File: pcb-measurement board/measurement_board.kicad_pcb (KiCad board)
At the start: 4 copper layers, 60 x 46 mm, 100 parts, among them P1 HDR DUAL ROW, P2 CONN_02X15, P3 CONN_02X13, P4 CONN_02X05, P5 CONN_02X05, Q1 Si1101X, Q2 2N7002, U1 NX3L4051, U10 TLV1G125, U11 NX3L4051, U12 MSP430G2955, U13 AD8603, U14 TLV1G125, U15 MCP4921, U16 AD8293, U17 NX3L4051, U18 NX3L4051, U19 QS4A110, U2 TPS73133, U20 QS4A110, U21 TLV1G125, U22 TLV1G125, U23 AD7683, U3 74CBTLV3253, U4 NX3L4051, U5 TPS73125, U6 AD8603, U7 MCP4921, U8 NX3L4051, U9 TLV1G125

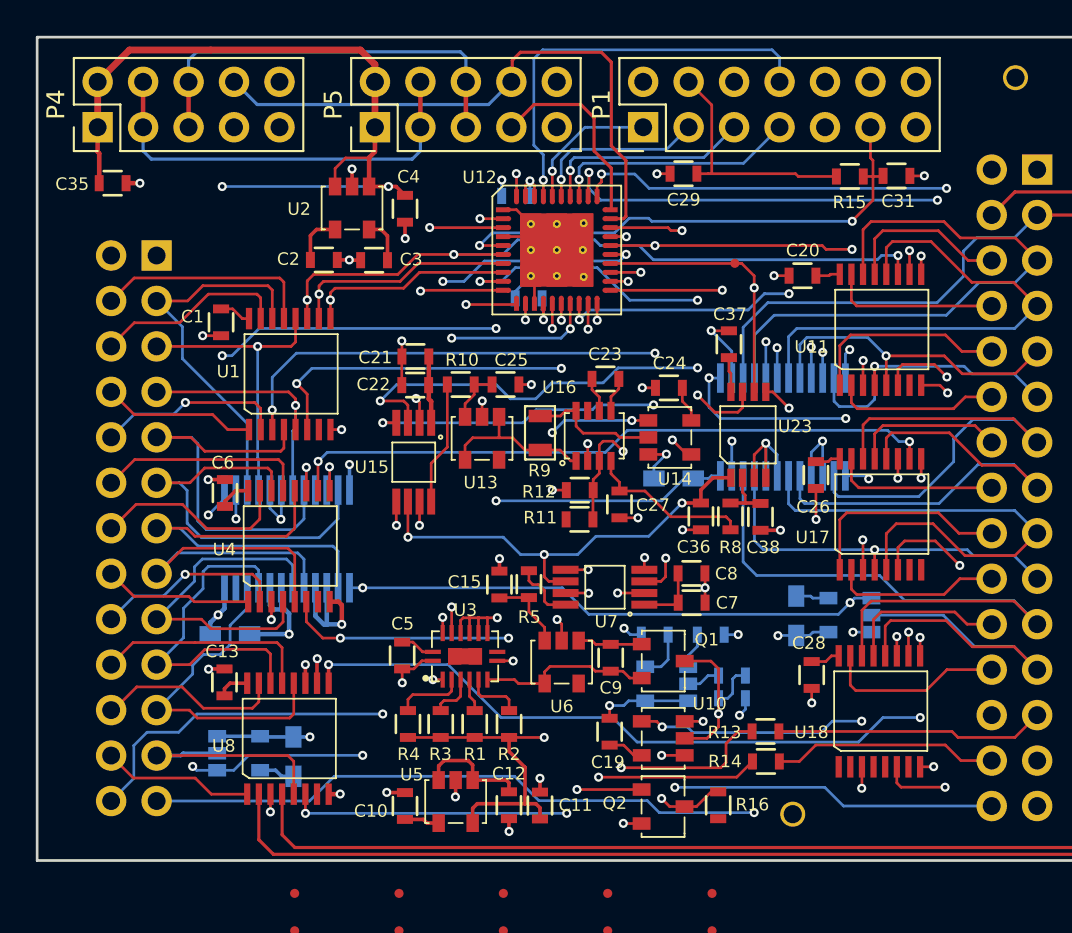
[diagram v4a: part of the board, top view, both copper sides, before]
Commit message: -nearing completion of measurement board layout -routed most signal traces, just need to add testpoints and fix DRC voilations -changed MSP430 programming connector from 2x7 header to 10-pin flex cable connector
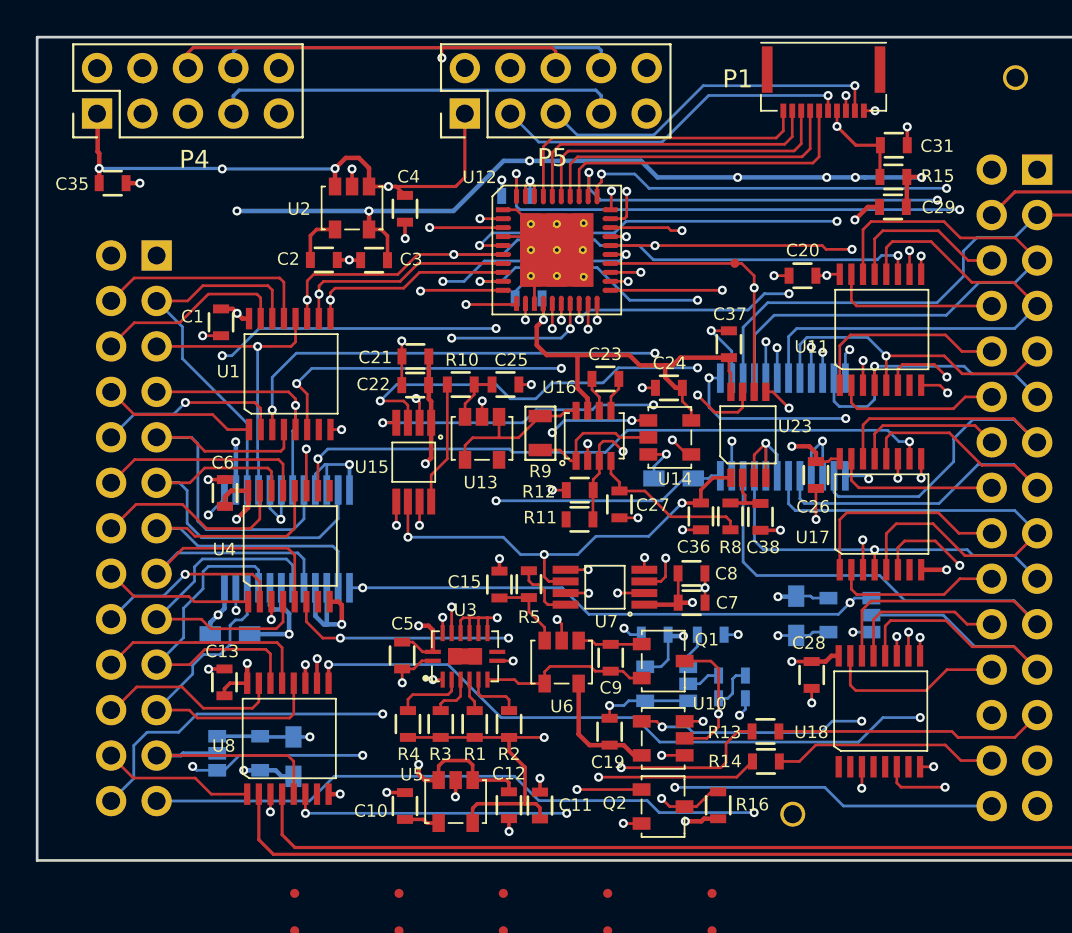
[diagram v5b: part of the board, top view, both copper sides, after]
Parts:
- C29: value 10uF -> 0.1uF
- P1: value HDR DUAL ROW -> 10-Pin Flex Cable; footprint Pin_Headers:Pin_Header_Straight_2x07_Pitch2.54mm -> WM6745-FPC
- P4, P5: footprint Pin_Headers:Pin_Header_Straight_2x05_Pitch2.54mm -> Footprints:header_2x5_idc
- moved C29 11.8 mm to (17.8, -15.5)
- moved P5 10.2 mm to (-1.13, -22.0), turned to 0 degrees
- moved P1 10.1 mm to (13.9, -20.9), turned to 180 degrees
- moved P4 5.34 mm to (-21.7, -22.0), turned to 0 degrees
- moved R15 2.43 mm to (17.8, -17.2)
- moved C31 1.72 mm to (17.9, -19.0)
- turned R9 to 90 degrees
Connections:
- P1 pad 1: /TDO -> GND
- P1 pad 10: Net-(P1-Pad10) -> /TEST
- P1 pad 2: Net-(P1-Pad2) -> /SCK
- P1 pad 3: /TDI -> /3V3
- P1 pad 4: /3V3 -> /~RST
- P1 pad 5: /TMS -> /SDA
- P1 pad 6: Net-(P1-Pad6) -> /TCK
- P1 pad 7: /TCK -> /TMS
- P1 pad 8: /TEST -> /TDI
- P1 pad 9: GND -> /TDO
- R15 pad 1: /~RST -> /3V3
- R15 pad 2: /3V3 -> /~RST
- U16 pad 1: Net-(R9-Pad2) -> Net-(R9-Pad1)
- U16 pad 8: Net-(R9-Pad1) -> Net-(R9-Pad2)
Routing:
- net /3V3: track 59.0 -> 275.6 mm, vias 2 -> 24
- net /SCK: track 36.2 -> 65.1 mm, vias 1 -> 3
- net /SDA: track 37.4 -> 66.2 mm, vias 1 -> 2
- net /~MUX_EN5: track 65.4 -> 53.2 mm, vias 2 -> 3
- net GND: track 126.7 -> 136.7 mm, vias 65 -> 68
- net /TDO: track 7.82 -> 17.6 mm, vias 1 -> 0
- net /TDI: track 9.86 -> 17.7 mm, vias 1 -> 0
- net /5V: track 109.5 -> 102.7 mm, vias 6 -> 8
- net /TMS: track 11.8 -> 17.6 mm, vias 1 -> 0
- net /TEST: track 23.3 -> 17.6 mm, vias 1 -> 0
- net /TCK: track 13.7 -> 17.7 mm, vias 1 -> 0
- net /~RST: track 29.7 -> 32.6 mm, vias 2 -> 3
- net /MUX2: track 98.7 -> 97.3 mm, vias 7 -> 6
- net /GPIO_B: track 33.5 -> 32.4 mm, vias 0 -> 1
- net /MUX0: track 86.6 -> 87.7 mm
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
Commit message: -layout of measurement board completed -gerber files created -added a pdf of the schematic
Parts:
- removed TP11, TP13, TP14, TP15, TP6, TP7: TP_SMT, footprints_on_Cdrive:TP_SMT.02
- added C39: 10pF, footprints_on_Cdrive:0402, F.Cu at (-4.14, -0.01)
- added C40: 0.1uF, footprints_on_Cdrive:0603, F.Cu at (0.31, 3.56)
- added R17: 0 ohm, footprints_on_Cdrive:0402, F.Cu at (-4.11, 2.99)
- added R18: DNI, footprints_on_Cdrive:0402, F.Cu at (-4.13, 1.76)
- P1: footprint WM6745-FPC -> footprints_on_Cdrive:WM6745-FPC
- P4, P5: footprint Footprints:header_2x5_idc -> footprints_on_Cdrive:header_2x5_idc
- moved TP8 45.5 mm to (-22.9, -16.7)
- moved TP9 44.3 mm to (-22.9, -15.1)
- moved TP1 42.9 mm to (-17.3, -16.0)
- moved TP12 42.4 mm to (7.53, -17.1)
- moved TP10 40.1 mm to (3.99, -17.2)
- moved TP3 28.5 mm to (-11.8, -3.36)
- moved TP4 24.5 mm to (2.89, 3.91)
- moved TP2 6.05 mm to (-4.59, 19.7)
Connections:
- R11 pad 2: /3V3 -> /V2P5
- R9 pad 2: Net-(R9-Pad2) -> Net-(C39-Pad1)
- TP3 pad 1: Net-(C15-Pad1) -> /DAC2_CS
- U13 pad 1: Net-(R9-Pad2) -> Net-(C39-Pad1)
- U13 pad 4: Net-(R9-Pad2) -> Net-(C39-Pad2)
- U16 pad 8: Net-(R9-Pad2) -> Net-(C39-Pad1)
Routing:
- net /3V3: track 275.6 -> 304.7 mm, vias 24 -> 26
- net Net-(C39-Pad1): track 0.00 -> 11.8 mm
- net Net-(R9-Pad2): track 9.55 -> 0.00 mm
- net Net-(C39-Pad2): track 0.00 -> 6.98 mm
- net /SCK: track 65.1 -> 71.3 mm
- net Net-(R17-Pad2): track 7.70 -> 13.9 mm
- net /DAC2_CS: track 15.4 -> 21.2 mm
- net /GPIO_B: track 32.4 -> 37.3 mm
- net /SDA: track 66.2 -> 71.1 mm
- net /V2P5: track 71.8 -> 76.4 mm
- net /GPIO_A: track 28.4 -> 30.9 mm
- net /DAC1_CS: track 20.8 -> 23.2 mm
- net /MUX2: track 97.3 -> 99.3 mm, vias 6 -> 7
- net /0V5: track 19.2 -> 20.8 mm
- net GND: track 136.7 -> 137.6 mm, vias 68 -> 69
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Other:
- board text added: "3V3"
- board text added: "A"
- board text added: "B"
- board text added: "C"
- board text added: "CLK"
- board text added: "D"
- board text added: "E"
- board text added: "F"
- board text added: "G"
- board text added: "GND"
- board text added: "H"
- board text added: "I"
- board text added: "IO_A"
- board text added: "IO_B"
- board text added: "J"
- board text added: "K"
- board text added: "L"
- board text added: "LED1"
- board text added: "LED2"
- board text added: "M"
- board text added: "N"
- board text added: "O"
- board text added: "P"
- board text added: "Q"
- board text added: "R"
- board text added: "S"
- board text added: "SCK"
- board text added: "SDA"
- board text added: "SIMO"
- board text added: "SOMI"
- board text added: "T"
- board text added: "U"
- board text added: "V"
- board text added: "V2P5"
- board text added: "~CS"
- board text added: "~CS1"
- board text added: "~CS2"
